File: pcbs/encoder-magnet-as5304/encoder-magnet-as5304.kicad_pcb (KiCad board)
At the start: 2 copper layers, 11.3 x 10.9 mm, 14 parts, among them J1 Conn_01x05, Q1 BC807-40LWX, U1 AS5304

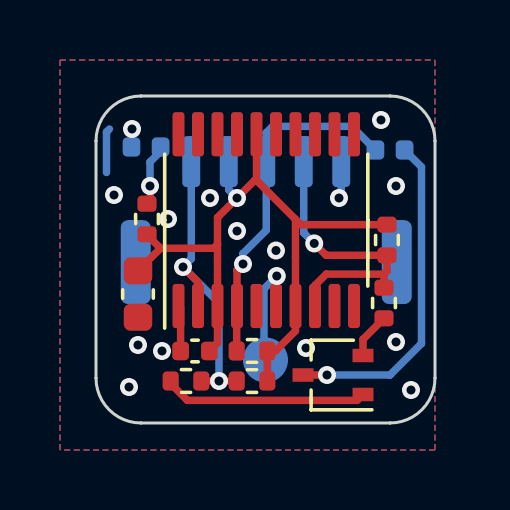
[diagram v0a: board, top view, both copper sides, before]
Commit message: Fix AS5304 board dimensions
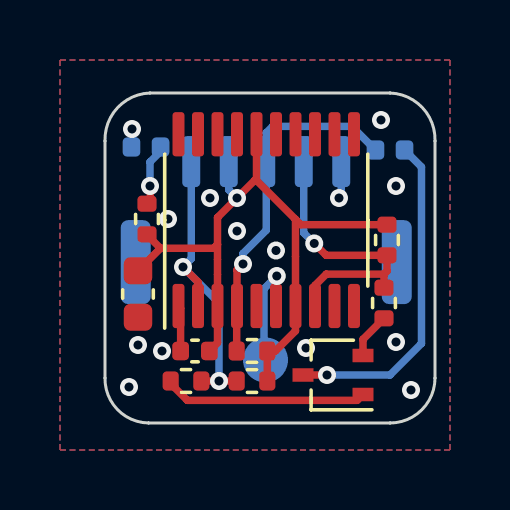
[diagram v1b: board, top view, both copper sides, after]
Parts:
- D1: value Warning -> Red
- D2: value +5V -> Blue
- J1: value Conn_01x05 -> BM05B-GHS
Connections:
- J1 pad MP: (no net) -> GND
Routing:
- net GND: track 4.87 -> 3.38 mm, vias 15 -> 14
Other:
- board size 11.3 x 10.9 mm -> 11 x 11 mm
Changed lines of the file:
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@@
       (net 1 "+5V") (pintype "passive"))
     (pad "2" smd roundrect locked (at 0.775 0 270) (size 0.9 0.95) (layers "F.Cu" "F.Paste" "F.Mask") (roundrect_rratio 0.25)
-      (net 2 "GND") (pintype "passive"))
+      (net 2 "GND") (pintype "passive") (zone_connect 2))
     (model "${KICAD6_3DMODEL_DIR}/Capacitor_SMD.3dshapes/C_0603_1608Metric.wrl"
       (offset (xyz 0 0 0))
@@
       (effects (font (size 1 1) (thickness 0.15)) (justify mirror))
     )
-    (fp_text value "+5V" (at 0 -1.17 180) (layer "B.Fab") hide
+    (fp_text value "Blue" (at 0 -1.17 180) (layer "B.Fab") hide
       (effects (font (size 1 1) (thickness 0.15)) (justify mirror))
     )
@@
     (fp_line (start 0.5 0.25) (end 0.5 -0.25) (layer "B.Fab") (width 0.1))
     (pad "1" smd roundrect locked (at -0.485 0) (size 0.59 0.64) (layers "B.Cu" "B.Paste" "B.Mask") (roundrect_rratio 0.25)
-      (net 2 "GND") (pinfunction "K") (pintype "passive"))
+      (net 2 "GND") (pinfunction "K") (pintype "passive") (zone_connect 2))
     (pad "2" smd roundrect locked (at 0.485 0) (size 0.59 0.64) (layers "B.Cu" "B.Paste" "B.Mask") (roundrect_rratio 0.25)
       (net 5 "Net-(D2-Pad2)") (pinfunction "A") (pintype "passive"))
@@
       (effects (font (size 1 1) (thickness 0.15)) (justify mirror))
     )
-    (fp_text value "Conn_01x05" (at 0 -4) (layer "B.Fab") hide
+    (fp_text value "BM05B-GHS" (at 0 -4) (layer "B.Fab") hide
       (effects (font (size 1 1) (thickness 0.15)) (justify mirror))
     )
@@
     (pad "5" smd roundrect locked (at 2.5 -1.95) (size 0.6 1.7) (layers "B.Cu" "B.Paste" "B.Mask") (roundrect_rratio 0.25)
       (net 2 "GND") (pinfunction "Pin_5") (pintype "passive"))
-    (pad "MP" smd roundrect locked (at -4.35 1.4) (size 1 2.8) (layers "B.Cu" "B.Paste" "B.Mask") (roundrect_rratio 0.25))
-    (pad "MP" smd roundrect locked (at 4.35 1.4) (size 1 2.8) (layers "B.Cu" "B.Paste" "B.Mask") (roundrect_rratio 0.25))
+    (pad "MP" smd roundrect locked (at -4.35 1.4) (size 1 2.8) (layers "B.Cu" "B.Paste" "B.Mask") (roundrect_rratio 0.25)
+      (net 2 "GND") (pinfunction "MountPin") (pintype "passive") (zone_connect 2))
+    (pad "MP" smd roundrect locked (at 4.35 1.4) (size 1 2.8) (layers "B.Cu" "B.Paste" "B.Mask") (roundrect_rratio 0.25)
+      (net 2 "GND") (pinfunction "MountPin") (pintype "passive") (zone_connect 2))
     (model "${KICAD6_3DMODEL_DIR}/Connector_JST.3dshapes/JST_GH_BM05B-GHS-TBT_1x05-1MP_P1.25mm_Vertical.wrl"
       (offset (xyz 0 0 0))
@@
       (effects (font (size 1 1) (thickness 0.15)) (justify mirror))
     )
-    (fp_text value "Warning" (at 0 -1.17 180) (layer "B.Fab") hide
+    (fp_text value "Red" (at 0 -1.17 180) (layer "B.Fab") hide
       (effects (font (size 1 1) (thickness 0.15)) (justify mirror))
     )
@@
       (net 20 "Net-(TP1-Pad1)") (pinfunction "1") (pintype "passive"))
   )
-  (gr_line (start 19.7 17.2) (end 28 17.2) (layer "Edge.Cuts") (width 0.1))
-  (gr_arc (start 29.5 26.6) (mid 29.06066 27.66066) (end 28 28.1) (layer "Edge.Cuts") (width 0.1))
+  (gr_line (start 20 17.1) (end 28 17.1) (layer "Edge.Cuts") (width 0.1))
+  (gr_arc (start 29.5 26.6) (mid 29.06066 27.660659) (end 28 28.1) (layer "Edge.Cuts") (width 0.1))
   (gr_line (start 29.5 18.7) (end 29.5 26.6) (layer "Edge.Cuts") (width 0.1))
-  (gr_arc (start 28 17.2) (mid 29.06066 17.63934) (end 29.5 18.7) (layer "Edge.Cuts") (width 0.1))
-  (gr_arc (start 18.2 18.7) (mid 18.63934 17.63934) (end 19.7 17.2) (layer "Edge.Cuts") (width 0.1))
-  (gr_arc (start 19.7 28.1) (mid 18.63934 27.66066) (end 18.2 26.6) (layer "Edge.Cuts") (width 0.1))
-  (gr_line (start 18.2 26.6) (end 18.2 18.7) (layer "Edge.Cuts") (width 0.1))
-  (gr_line (start 28 28.1) (end 19.7 28.1) (layer "Edge.Cuts") (width 0.1))
+  (gr_arc (start 28 17.1) (mid 29.08137 17.58934) (end 29.5 18.7) (layer "Edge.Cuts") (width 0.1))
+  (gr_arc (start 19.95 28.1) (mid 18.91434 27.650305) (end 18.5 26.6) (layer "Edge.Cuts") (width 0.1))
+  (gr_line (start 18.5 26.6) (end 18.5 18.7) (layer "Edge.Cuts") (width 0.1))
+  (gr_line (start 28 28.1) (end 19.95 28.1) (layer "Edge.Cuts") (width 0.1))
+  (gr_arc (start 18.5 18.7) (mid 18.918629 17.58934) (end 20 17.1) (layer "Edge.Cuts") (width 0.1))
   (dimension (type aligned) (layer "Dwgs.User")
-    (pts (xy 23.9 17.2) (xy 23.9 28.1))
-    (height -8.7)
-    (gr_text "10,9000 mm" (at 31.45 22.65 90) (layer "Dwgs.User")
+    (pts (xy 18.5 22.65) (xy 29.5 22.65))
+    (height 9.05)
+    (gr_text "11,0000 mm" (at 24 30.55) (layer "Dwgs.User")
       (effects (font (size 1 1) (thickness 0.15)))
     )
     (format (units 3) (units_format 1) (precision 4))
-    (style (thickness 0.15) (arrow_length 1.27) (text_position_mode 0) (extension_height 0.58642) (extension_offset 0.5) keep_text_aligned)
+    (style (thickness 0.1) (arrow_length 1.27) (text_position_mode 0) (extension_height 0.58642) (extension_offset 0.5) keep_text_aligned)
   )
   (dimension (type aligned) (layer "Dwgs.User")
-    (pts (xy 18.2 25) (xy 29.5 25))
-    (height 6.4)
-    (gr_text "11,3000 mm" (at 23.85 30.25) (layer "Dwgs.User")
+    (pts (xy 24 17.1) (xy 23.975 28.1))
+    (height -11.925878)
+    (gr_text "11,0000 mm" (at 34.76335 22.62449 89.86978254) (layer "Dwgs.User")
       (effects (font (size 1 1) (thickness 0.15)))
     )
@@
   (via (at 22.9 21.7) (size 0.6) (drill 0.3) (layers "F.Cu" "B.Cu") (free) (net 2))
   (via (at 28.2 20.2) (size 0.6) (drill 0.3) (layers "F.Cu" "B.Cu") (free) (net 2))
-  (via (at 18.8 20.5) (size 0.6) (drill 0.3) (layers "F.Cu" "B.Cu") (free) (net 2))
   (via (at 19.6 25.5) (size 0.6) (drill 0.3) (layers "F.Cu" "B.Cu") (free) (net 2))
   (via (at 28.7 27) (size 0.6) (drill 0.3) (layers "F.Cu" "B.Cu") (free) (net 2))
@@
   (segment (start 19.415 18.9) (end 19.415 18.315) (width 0.25) (layer "B.Cu") (net 2))
   (segment (start 19.415 18.315) (end 19.4 18.3) (width 0.25) (layer "B.Cu") (net 2))
-  (segment (start 18.55 18.4) (end 18.65 18.3) (width 0.25) (layer "B.Cu") (net 2))
   (segment (start 26.375 20.525) (end 26.3 20.6) (width 0.25) (layer "B.Cu") (net 2))
-  (segment (start 18.55 19.75) (end 18.55 18.4) (width 0.25) (layer "B.Cu") (net 2))
   (segment (start 22.89 24.21) (end 22.9 24.2) (width 0.25) (layer "F.Cu") (net 3))
   (segment (start 22.9 24.2) (end 22.9 23) (width 0.25) (layer "F.Cu") (net 3))
@@
     (polygon
       (pts
-        (xy 29.5 29)
+        (xy 30 29)
         (xy 17 29)
         (xy 17 16)
-        (xy 29.5 16)
+        (xy 30 16)
       )
     )
